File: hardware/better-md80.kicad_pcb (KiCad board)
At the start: 6 copper layers, 56.7 x 54.7 mm, 145 parts, among them J1 Micro-Fit 2x3, J10 Phase A, J11 Phase B, J12 Phase C, J2 Micro-Fit 2x3, J3 AUX1 SPI enc, J4 AUX2 RS422, J5 Motor NTC, J6 TC2030-NL, K1 CPC1017N, Q1 ISC022N10NM6, Q2 ISC022N10NM6, Q3 ISC022N10NM6, Q4 ISC022N10NM6, Q5 ISC022N10NM6, Q6 ISC022N10NM6, U1 LM5164DDAR, U2 TPS62163DSGR, U3 TLV75533PDBVR, U4 DRV8353SRTAR, U5 STM32G474CEU6, U6 TCAN1044AVDR, U7 AS5047P-ATSM, U8 MAX3490EESA+, Y1 8MHz

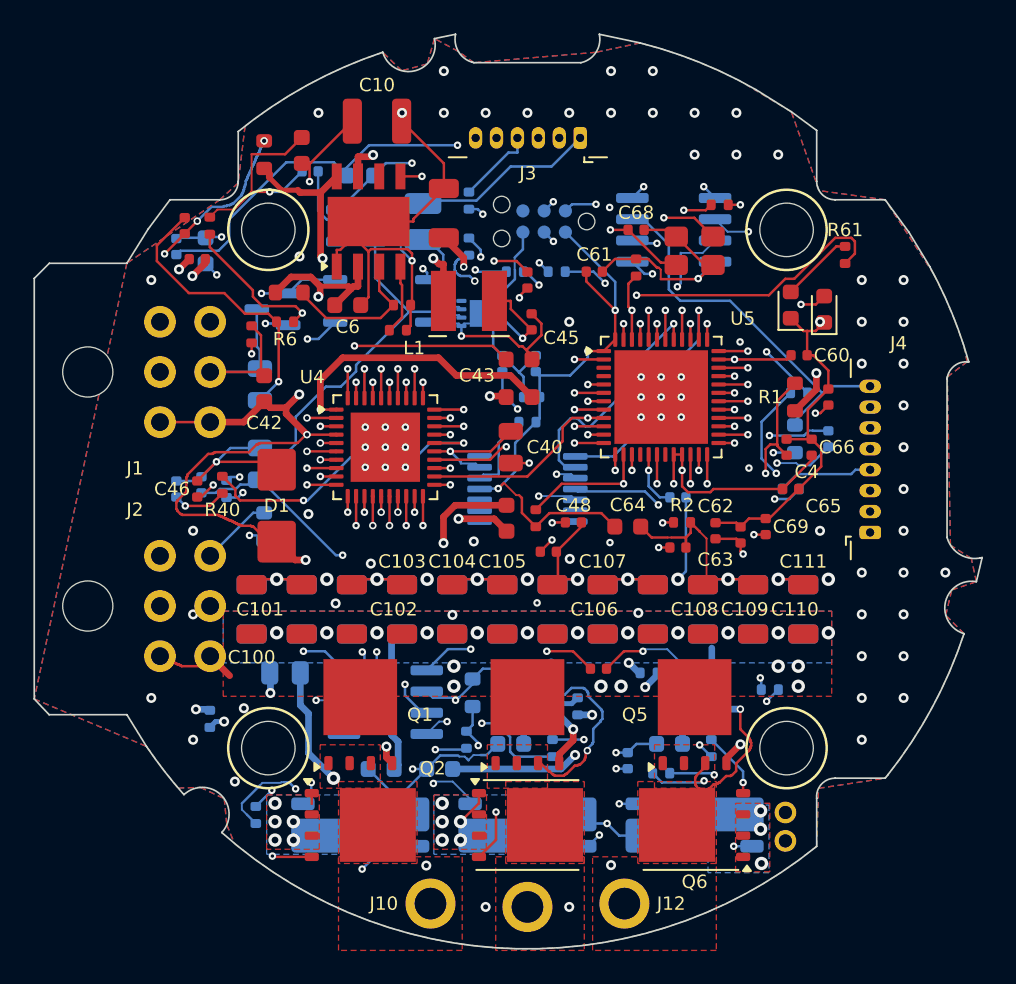
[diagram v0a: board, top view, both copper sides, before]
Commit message: Layout rev B: top-side two-shunt power stage, 5.0SMDJ60A TVS, crystal by the MCU
Commutation loop 5.0 -> 3.0 nH (FastHenry), 60 V hot-plug peak 106 -> 96 V.
Re-placed and re-routed (Freerouting + tools/hand_route.py); DRC: 0 unconnected,
only the MD80-inherent AUX1/screw courtyard overlap. Docs and sims updated.

Co-Authored-By: Claude Opus 5.5 (1M context) <noreply@anthropic.com>
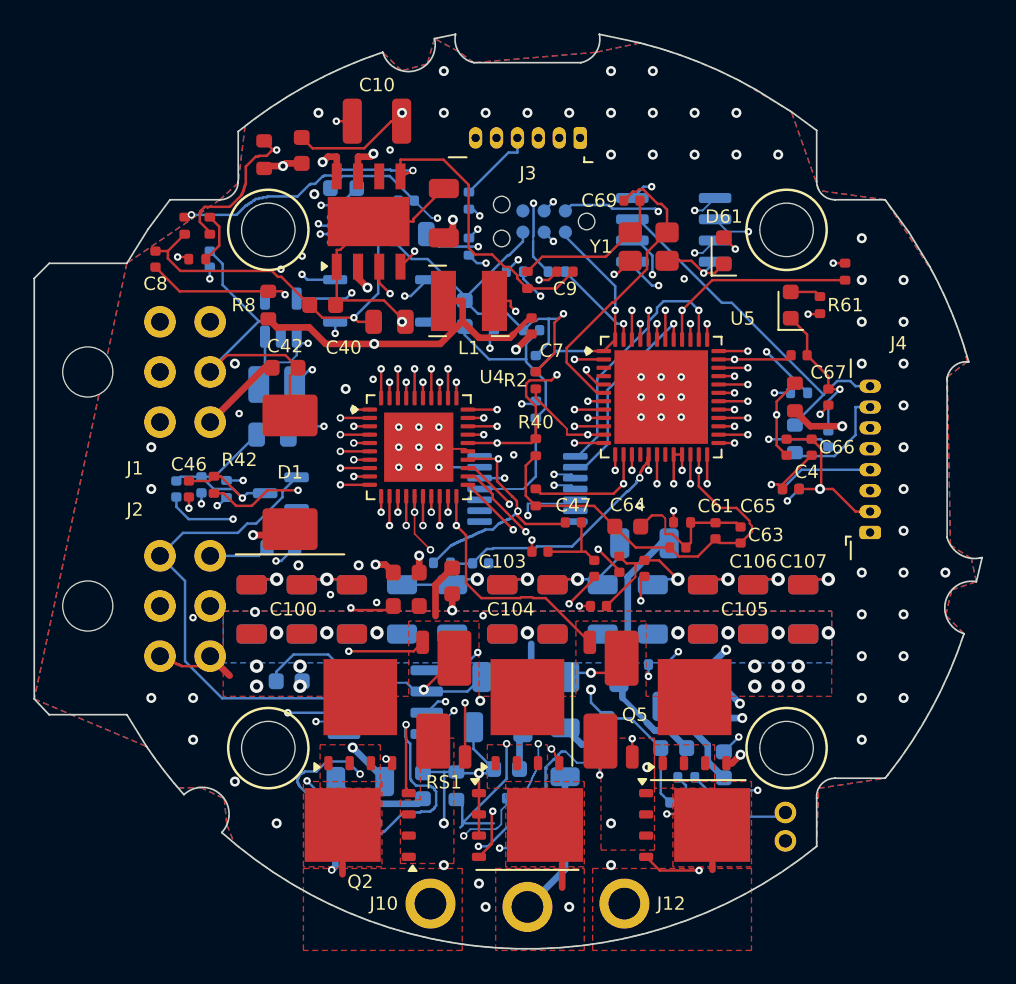
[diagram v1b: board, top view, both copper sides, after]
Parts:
- removed RS2: 0.5m, Resistor_SMD:R_Shunt_Vishay_WSK2512_6332Metric_T2.66mm
- C108, C109, C110, C111: moved to B.Cu
- D1: value SMBJ60A -> 5.0SMDJ60A; footprint Diode_SMD:D_SMB -> Diode_SMD:D_SMC
- R30, R31, R32: footprint Resistor_SMD:R_0805_2012Metric -> Resistor_SMD:R_1206_3216Metric
- RS1, RS3: moved to F.Cu
- moved C69 21.1 mm to (156.2, 82.8), turned to 0 degrees
- moved C7 20.4 mm to (150.2, 90.2), turned to 90 degrees
- moved C68 20.3 mm to (157.0, 104.8), turned to 90 degrees
- moved C111 19.6 mm to (148.2, 114.2), turned to 180 degrees
- moved R7 19.3 mm to (150.0, 87.5)
- moved R40 18.9 mm to (150.5, 97.5)
- moved C61 17.1 mm to (161.2, 102.5), turned to 90 degrees
- moved C13 16.4 mm to (143.0, 84.8), turned to 180 degrees
- moved C45 16.2 mm to (142.8, 107.0)
- moved C15 15.9 mm to (146.2, 89.5)
- moved R60 15.5 mm to (159.2, 102.0), turned to 0 degrees
- moved C16 14.0 mm to (142.8, 82.8), turned to 180 degrees
- moved C41 13.8 mm to (150.8, 103.8), turned to 0 degrees
- moved L2 13.1 mm to (135.0, 93.8), turned to 180 degrees
- moved R5 12.7 mm to (130.2, 86.2)
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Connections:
- Q4 pad 1: LSB -> GND
- Q4 pad 2: LSB -> GND
- Q4 pad 3: LSB -> GND
- U4 pad 11: SNB -> GND
- U4 pad 12: SPB -> GND
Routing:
- net TEMP_FET: track 27.0 -> 57.4 mm, vias 2 -> 3
- net DRV_nFAULT: track 50.7 -> 22.1 mm
- net SNB: track 28.4 -> 0.00 mm, vias 2 -> 0
- net SNUBA: track 28.7 -> 5.89 mm, vias 2 -> 0
- net +5V: track 100.0 -> 122.6 mm, vias 2 -> 6
- net SPB: track 22.2 -> 0.00 mm, vias 2 -> 0
- net INHA: track 40.4 -> 22.2 mm
- net UVLO12: track 9.11 -> 26.9 mm, vias 0 -> 3
- net CAN_TX: track 48.1 -> 32.0 mm
- net HSE_OUT: track 32.8 -> 18.0 mm, vias 3 -> 0
- net SNA: track 30.1 -> 16.6 mm
- net GLC_G: track 3.99 -> 17.1 mm, vias 1 -> 2
- net RON12: track 4.15 -> 16.9 mm, vias 0 -> 4
- net DRV_EN: track 51.7 -> 39.4 mm
- net PHB: track 39.0 -> 27.5 mm, vias 5 -> 1
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- removed copper zone on B.Cu, net LSA
- removed copper zone on B.Cu, net LSB
- removed copper zone on F.Cu, net LSB
- removed copper zone on B.Cu, net LSC
